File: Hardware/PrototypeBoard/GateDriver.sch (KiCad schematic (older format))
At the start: 38 parts, among them U4 TLE7185-1E

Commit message: continued to work on new layout
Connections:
- net Source_V_L: now also U4.24 (SL2)
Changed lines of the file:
@@
 Wire Wire Line
 	6950 3700 7300 3700
+Wire Wire Line
+	5700 4800 6300 4800
 $EndSCHEMATC

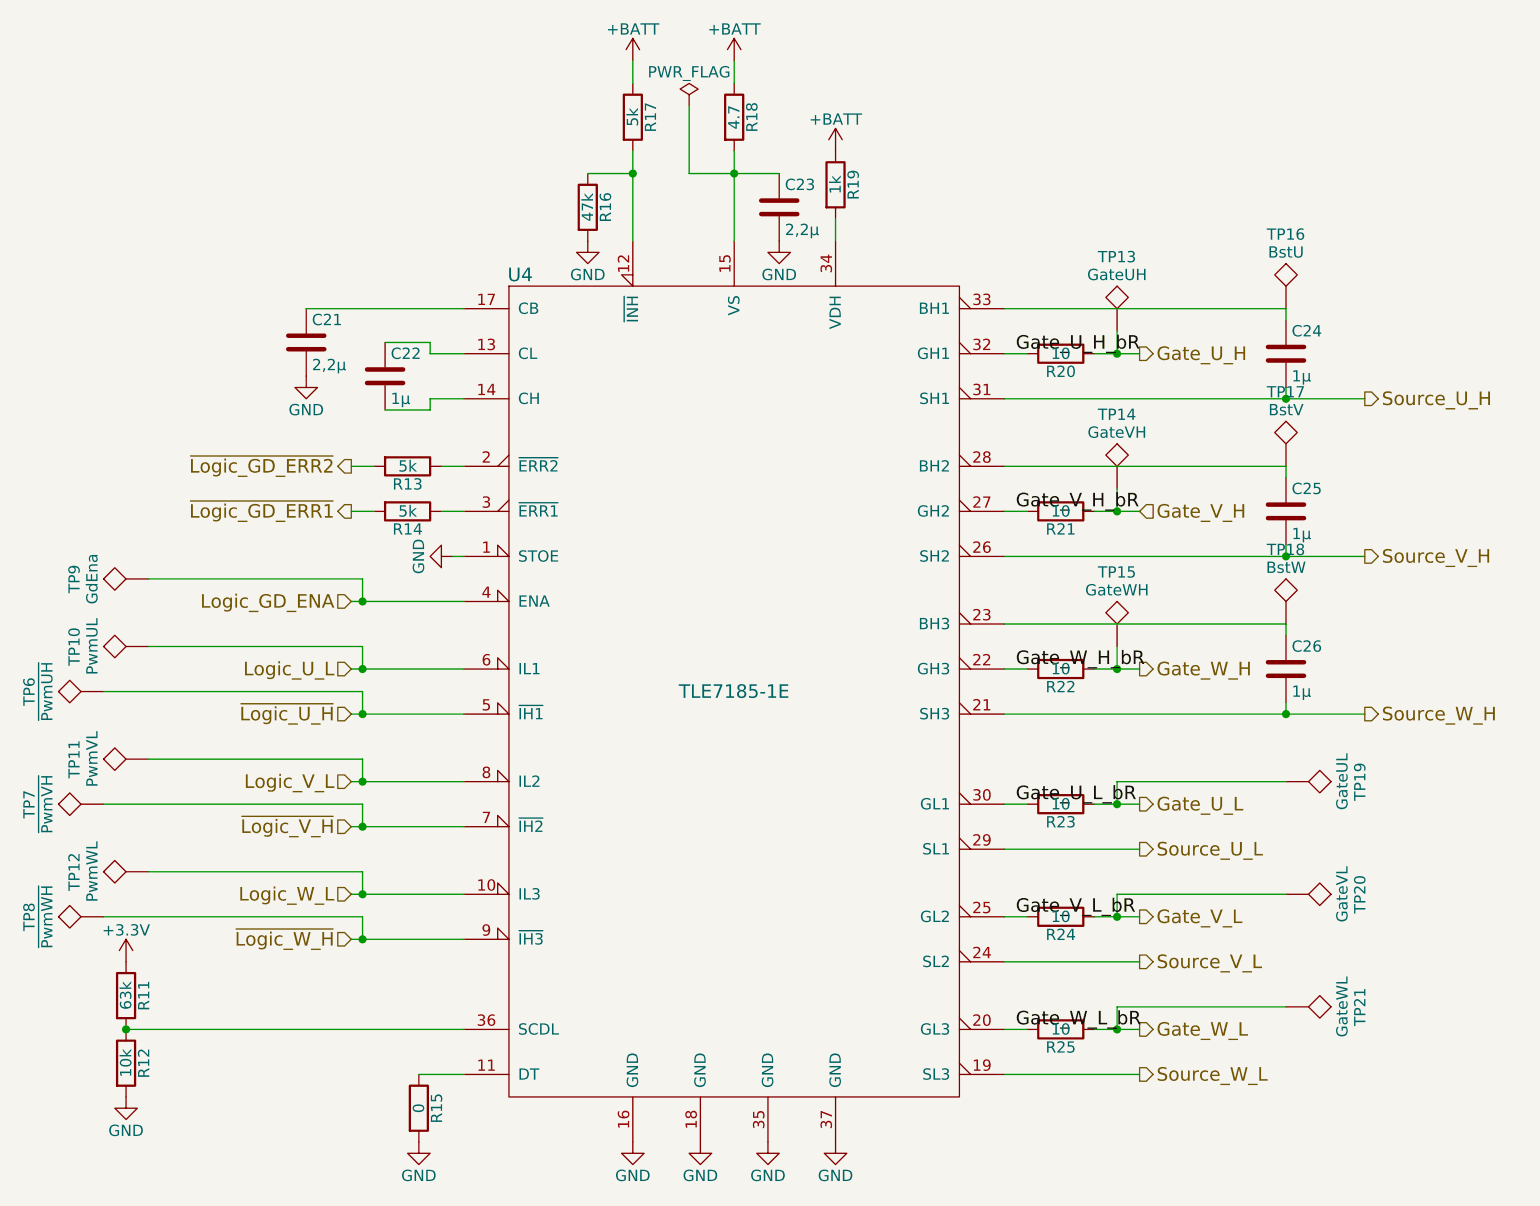
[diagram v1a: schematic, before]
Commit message: Added LEDs for PWM, SPI communication, Gate Driver Errors and Gate Driver disabled
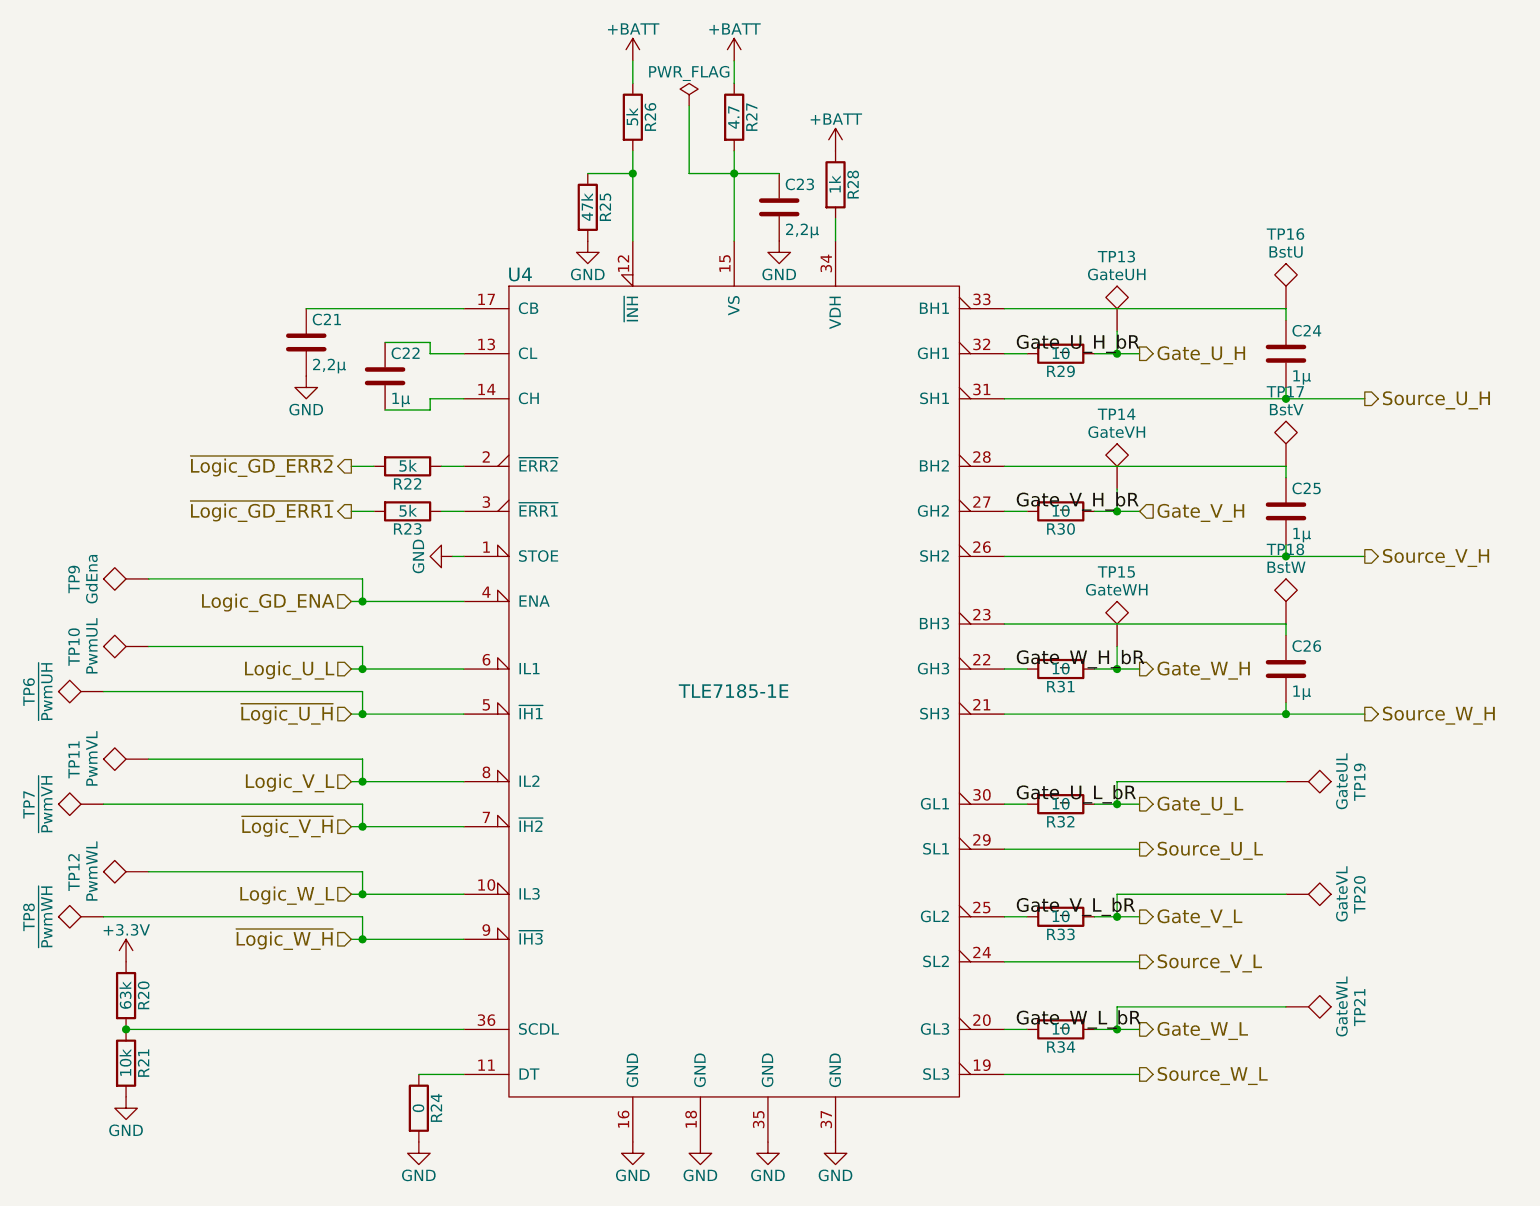
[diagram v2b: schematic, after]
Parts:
- renumbered R11 to R20, R12 to R21, R13 to R22, R14 to R23, R15 to R24, R16 to R25, R17 to R26, R18 to R27, R19 to R28, R20 to R29, R21 to R30, R22 to R31, R23 to R32, R24 to R33, R25 to R34
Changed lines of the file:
@@
 Logic_GD_ENA
 $Comp
-L Device:R R14
+L Device:R R23
 U 1 1 56C25790
 P 3050 2800
-F 0 "R14" V 3130 2800 50  0000 C CNN
+F 0 "R23" V 3130 2800 50  0000 C CNN
 F 1 "5k" V 3050 2800 50  0000 C CNN
 F 2 "Resistors_SMD:R_0805_HandSoldering" V 2980 2800 50  0001 C CNN
@@
 $EndComp
 $Comp
-L Device:R R13
+L Device:R R22
 U 1 1 56C257FB
 P 3050 2600
-F 0 "R13" V 3130 2600 50  0000 C CNN
+F 0 "R22" V 3130 2600 50  0000 C CNN
 F 1 "5k" V 3050 2600 50  0000 C CNN
 F 2 "Resistors_SMD:R_0805_HandSoldering" V 2980 2600 50  0001 C CNN
@@
 	2600 1900 3300 1900
 $Comp
-L power:GND #PWR038
+L power:GND #PWR044
 U 1 1 56C259AC
 P 2600 2200
-F 0 "#PWR038" H 2600 1950 50  0001 C CNN
+F 0 "#PWR044" H 2600 1950 50  0001 C CNN
 F 1 "GND" H 2600 2050 50  0000 C CNN
 F 2 "" H 2600 2200 50  0000 C CNN
@@
 $EndComp
 $Comp
-L Device:R R11
+L Device:R R20
 U 1 1 56C25A1A
 P 1800 4950
-F 0 "R11" V 1880 4950 50  0000 C CNN
+F 0 "R20" V 1880 4950 50  0000 C CNN
 F 1 "63k" V 1800 4950 50  0000 C CNN
 F 2 "Resistors_SMD:R_0805_HandSoldering" V 1730 4950 50  0001 C CNN
@@
 $EndComp
 $Comp
-L Device:R R12
+L Device:R R21
 U 1 1 56C25AD5
 P 1800 5250
-F 0 "R12" V 1880 5250 50  0000 C CNN
+F 0 "R21" V 1880 5250 50  0000 C CNN
 F 1 "10k" V 1800 5250 50  0000 C CNN
 F 2 "Resistors_SMD:R_0805_HandSoldering" V 1730 5250 50  0001 C CNN
@@
 $EndComp
 $Comp
-L Device:R R15
+L Device:R R24
 U 1 1 56C25B0C
 P 3100 5450
-F 0 "R15" V 3180 5450 50  0000 C CNN
+F 0 "R24" V 3180 5450 50  0000 C CNN
 F 1 "0" V 3100 5450 50  0000 C CNN
 F 2 "Resistors_SMD:R_0805_HandSoldering" V 3030 5450 50  0001 C CNN
@@
 	3300 5300 3100 5300
 $Comp
-L power:GND #PWR037
+L power:GND #PWR043
 U 1 1 56C25C22
 P 1800 5400
-F 0 "#PWR037" H 1800 5150 50  0001 C CNN
+F 0 "#PWR043" H 1800 5150 50  0001 C CNN
 F 1 "GND" H 1800 5250 50  0000 C CNN
 F 2 "" H 1800 5400 50  0000 C CNN
@@
 $EndComp
 $Comp
-L power:GND #PWR039
+L power:GND #PWR045
 U 1 1 56C25CA5
 P 3100 5600
-F 0 "#PWR039" H 3100 5350 50  0001 C CNN
+F 0 "#PWR045" H 3100 5350 50  0001 C CNN
 F 1 "GND" H 3100 5450 50  0000 C CNN
 F 2 "" H 3100 5600 50  0000 C CNN
@@
 $EndComp
 $Comp
-L power:+3.3V #PWR036
+L power:+3.3V #PWR042
 U 1 1 56C25D62
 P 1800 4800
-F 0 "#PWR036" H 1800 4650 50  0001 C CNN
+F 0 "#PWR042" H 1800 4650 50  0001 C CNN
 F 1 "+3.3V" H 1800 4940 50  0000 C CNN
 F 2 "" H 1800 4800 50  0000 C CNN
@@
 $EndComp
 $Comp
-L Device:R R18
+L Device:R R27
 U 1 1 56C25E1E
 P 4500 1050
-F 0 "R18" V 4580 1050 50  0000 C CNN
+F 0 "R27" V 4580 1050 50  0000 C CNN
 F 1 "4.7" V 4500 1050 50  0000 C CNN
 F 2 "Resistors_SMD:R_0805_HandSoldering" V 4430 1050 50  0001 C CNN
@@
 $EndComp
 $Comp
-L power:GND #PWR047
+L power:GND #PWR053
 U 1 1 56C2602E
 P 4700 1600
-F 0 "#PWR047" H 4700 1350 50  0001 C CNN
+F 0 "#PWR053" H 4700 1350 50  0001 C CNN
 F 1 "GND" H 4700 1450 50  0000 C CNN
 F 2 "" H 4700 1600 50  0000 C CNN
@@
 $EndComp
 $Comp
-L power:+BATT #PWR045
+L power:+BATT #PWR051
 U 1 1 56C261FD
 P 4500 800
-F 0 "#PWR045" H 4500 650 50  0001 C CNN
+F 0 "#PWR051" H 4500 650 50  0001 C CNN
 F 1 "+BATT" H 4500 940 50  0000 C CNN
 F 2 "" H 4500 800 50  0000 C CNN
@@
 $EndComp
 $Comp
-L Device:R R19
+L Device:R R28
 U 1 1 56C26356
 P 4950 1350
-F 0 "R19" V 5030 1350 50  0000 C CNN
+F 0 "R28" V 5030 1350 50  0000 C CNN
 F 1 "1k" V 4950 1350 50  0000 C CNN
 F 2 "Resistors_SMD:R_0805_HandSoldering" V 4880 1350 50  0001 C CNN
@@
 	4950 1500 4950 1600
 $Comp
-L power:+BATT #PWR048
+L power:+BATT #PWR054
 U 1 1 56C26408
 P 4950 1200
-F 0 "#PWR048" H 4950 1050 50  0001 C CNN
+F 0 "#PWR054" H 4950 1050 50  0001 C CNN
 F 1 "+BATT" H 4950 1340 50  0000 C CNN
 F 2 "" H 4950 1200 50  0000 C CNN
@@
 Gate_W_L
 $Comp
-L Device:R R25
+L Device:R R34
 U 1 1 56C2703F
 P 5950 5100
-F 0 "R25" V 6030 5100 50  0000 C CNN
+F 0 "R34" V 6030 5100 50  0000 C CNN
 F 1 "10" V 5950 5100 50  0000 C CNN
 F 2 "Resistors_SMD:R_0805_HandSoldering" V 5880 5100 50  0001 C CNN
@@
 $EndComp
 $Comp
-L Device:R R24
+L Device:R R33
 U 1 1 56C271C9
 P 5950 4600
-F 0 "R24" V 6030 4600 50  0000 C CNN
+F 0 "R33" V 6030 4600 50  0000 C CNN
 F 1 "10" V 5950 4600 50  0000 C CNN
 F 2 "Resistors_SMD:R_0805_HandSoldering" V 5880 4600 50  0001 C CNN
@@
 Gate_U_L
 $Comp
-L Device:R R23
+L Device:R R32
 U 1 1 56C27221
 P 5950 4100
-F 0 "R23" V 6030 4100 50  0000 C CNN
+F 0 "R32" V 6030 4100 50  0000 C CNN
 F 1 "10" V 5950 4100 50  0000 C CNN
 F 2 "Resistors_SMD:R_0805_HandSoldering" V 5880 4100 50  0001 C CNN
@@
 $EndComp
 $Comp
-L Device:R R22
+L Device:R R31
 U 1 1 56C2752F
 P 5950 3500
-F 0 "R22" V 6030 3500 50  0000 C CNN
+F 0 "R31" V 6030 3500 50  0000 C CNN
 F 1 "10" V 5950 3500 50  0000 C CNN
 F 2 "Resistors_SMD:R_0805_HandSoldering" V 5880 3500 50  0001 C CNN
@@
 $EndComp
 $Comp
-L Device:R R21
+L Device:R R30
 U 1 1 56C2759F
 P 5950 2800
-F 0 "R21" V 6030 2800 50  0000 C CNN
+F 0 "R30" V 6030 2800 50  0000 C CNN
 F 1 "10" V 5950 2800 50  0000 C CNN
 F 2 "Resistors_SMD:R_0805_HandSoldering" V 5880 2800 50  0001 C CNN
@@
 $EndComp
 $Comp
-L Device:R R20
+L Device:R R29
 U 1 1 56C27617
 P 5950 2100
-F 0 "R20" V 6030 2100 50  0000 C CNN
+F 0 "R29" V 6030 2100 50  0000 C CNN
 F 1 "10" V 5950 2100 50  0000 C CNN
 F 2 "Resistors_SMD:R_0805_HandSoldering" V 5880 2100 50  0001 C CNN
@@
 $EndComp
 $Comp
-L power:GND #PWR043
+L power:GND #PWR049
 U 1 1 56C35C82
 P 4050 5600
-F 0 "#PWR043" H 4050 5350 50  0001 C CNN
+F 0 "#PWR049" H 4050 5350 50  0001 C CNN
 F 1 "GND" H 4050 5450 50  0000 C CNN
 F 2 "" H 4050 5600 50  0000 C CNN
@@
 $EndComp
 $Comp
-L power:GND #PWR044
+L power:GND #PWR050
 U 1 1 56C35CC9
 P 4350 5600
-F 0 "#PWR044" H 4350 5350 50  0001 C CNN
+F 0 "#PWR050" H 4350 5350 50  0001 C CNN
 F 1 "GND" H 4350 5450 50  0000 C CNN
 F 2 "" H 4350 5600 50  0000 C CNN
@@
 $EndComp
 $Comp
-L power:GND #PWR046
+L power:GND #PWR052
 U 1 1 56C35D10
 P 4650 5600
-F 0 "#PWR046" H 4650 5350 50  0001 C CNN
+F 0 "#PWR052" H 4650 5350 50  0001 C CNN
 F 1 "GND" H 4650 5450 50  0000 C CNN
 F 2 "" H 4650 5600 50  0000 C CNN
@@
 $EndComp
 $Comp
-L power:GND #PWR049
+L power:GND #PWR055
 U 1 1 56C35D57
 P 4950 5600
-F 0 "#PWR049" H 4950 5350 50  0001 C CNN
+F 0 "#PWR055" H 4950 5350 50  0001 C CNN
 F 1 "GND" H 4950 5450 50  0000 C CNN
 F 2 "" H 4950 5600 50  0000 C CNN
@@
 $EndComp
 $Comp
-L Device:R R16
+L Device:R R25
 U 1 1 56C36A2B
 P 3850 1450
-F 0 "R16" V 3930 1450 50  0000 C CNN
+F 0 "R25" V 3930 1450 50  0000 C CNN
 F 1 "47k" V 3850 1450 50  0000 C CNN
 F 2 "Resistors_SMD:R_0805_HandSoldering" V 3780 1450 50  0001 C CNN
@@
 $EndComp
 $Comp
-L power:GND #PWR041
+L power:GND #PWR047
 U 1 1 56C36B52
 P 3850 1600
-F 0 "#PWR041" H 3850 1350 50  0001 C CNN
+F 0 "#PWR047" H 3850 1350 50  0001 C CNN
 F 1 "GND" H 3850 1450 50  0000 C CNN
 F 2 "" H 3850 1600 50  0000 C CNN
@@
 $EndComp
 $Comp
-L Device:R R17
+L Device:R R26
 U 1 1 56C36CC4
 P 4050 1050
-F 0 "R17" V 4130 1050 50  0000 C CNN
+F 0 "R26" V 4130 1050 50  0000 C CNN
 F 1 "5k" V 4050 1050 50  0000 C CNN
 F 2 "Resistors_SMD:R_0805_HandSoldering" V 3980 1050 50  0001 C CNN
@@
 $EndComp
 $Comp
-L power:+BATT #PWR042
+L power:+BATT #PWR048
 U 1 1 56C36FE8
 P 4050 800
-F 0 "#PWR042" H 4050 650 50  0001 C CNN
+F 0 "#PWR048" H 4050 650 50  0001 C CNN
 F 1 "+BATT" H 4050 940 50  0000 C CNN
 F 2 "" H 4050 800 50  0000 C CNN
@@
 Gate_U_H
 $Comp
-L power:GND #PWR040
+L power:GND #PWR046
 U 1 1 5AFC4218
 P 3250 3000
-F 0 "#PWR040" H 3250 2750 50  0001 C CNN
+F 0 "#PWR046" H 3250 2750 50  0001 C CNN
 F 1 "GND" H 3250 2850 50  0000 C CNN
 F 2 "" H 3250 3000 50  0000 C CNN

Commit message: All tracks routed, fixed bug in schematic, smaller test points
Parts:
- TP10, TP11, TP12, TP13, TP14, TP15, TP16, TP17, TP18, TP19, TP20, TP21, TP6, TP7, TP8, TP9: footprint Pin_Headers:Pin_Header_Straight_1x01_Pitch2.00mm -> Pin_Headers:Pin_Header_Straight_1x01_Pitch1.00mm
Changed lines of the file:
@@
 F 0 "TP17" H 6950 2900 50  0000 C BNN
 F 1 "BstV" H 6950 2850 50  0000 C CNN
-F 2 "Pin_Headers:Pin_Header_Straight_1x01_Pitch2.00mm" H 6950 2600 50  0001 C CNN
+F 2 "Pin_Headers:Pin_Header_Straight_1x01_Pitch1.00mm" H 6950 2600 50  0001 C CNN
 F 3 "" H 6950 2600 50  0001 C CNN
 	1    6950 2600
@@
 F 0 "TP16" H 6950 2200 50  0000 C BNN
 F 1 "BstU" H 6950 2150 50  0000 C CNN
-F 2 "Pin_Headers:Pin_Header_Straight_1x01_Pitch2.00mm" H 6950 1900 50  0001 C CNN
+F 2 "Pin_Headers:Pin_Header_Straight_1x01_Pitch1.00mm" H 6950 1900 50  0001 C CNN
 F 3 "" H 6950 1900 50  0001 C CNN
 	1    6950 1900
@@
 F 0 "TP18" H 6950 3600 50  0000 C BNN
 F 1 "BstW" H 6950 3550 50  0000 C CNN
-F 2 "Pin_Headers:Pin_Header_Straight_1x01_Pitch2.00mm" H 6950 3300 50  0001 C CNN
+F 2 "Pin_Headers:Pin_Header_Straight_1x01_Pitch1.00mm" H 6950 3300 50  0001 C CNN
 F 3 "" H 6950 3300 50  0001 C CNN
 	1    6950 3300
@@
 F 0 "TP14" H 6200 3000 50  0000 C BNN
 F 1 "GateVH" H 6200 2950 50  0000 C CNN
-F 2 "Pin_Headers:Pin_Header_Straight_1x01_Pitch2.00mm" H 6200 2700 50  0001 C CNN
+F 2 "Pin_Headers:Pin_Header_Straight_1x01_Pitch1.00mm" H 6200 2700 50  0001 C CNN
 F 3 "" H 6200 2700 50  0001 C CNN
 	1    6200 2700
@@
 F 0 "TP13" H 6200 2300 50  0000 C BNN
 F 1 "GateUH" H 6200 2250 50  0000 C CNN
-F 2 "Pin_Headers:Pin_Header_Straight_1x01_Pitch2.00mm" H 6200 2000 50  0001 C CNN
+F 2 "Pin_Headers:Pin_Header_Straight_1x01_Pitch1.00mm" H 6200 2000 50  0001 C CNN
 F 3 "" H 6200 2000 50  0001 C CNN
 	1    6200 2000
@@
 F 0 "TP15" H 6200 3700 50  0000 C BNN
 F 1 "GateWH" H 6200 3650 50  0000 C CNN
-F 2 "Pin_Headers:Pin_Header_Straight_1x01_Pitch2.00mm" H 6200 3400 50  0001 C CNN
+F 2 "Pin_Headers:Pin_Header_Straight_1x01_Pitch1.00mm" H 6200 3400 50  0001 C CNN
 F 3 "" H 6200 3400 50  0001 C CNN
 	1    6200 3400
@@
 F 0 "TP19" H 6950 4300 50  0000 C BNN
 F 1 "GateUL" H 6950 4250 50  0000 C CNN
-F 2 "Pin_Headers:Pin_Header_Straight_1x01_Pitch2.00mm" H 6950 4000 50  0001 C CNN
+F 2 "Pin_Headers:Pin_Header_Straight_1x01_Pitch1.00mm" H 6950 4000 50  0001 C CNN
 F 3 "" H 6950 4000 50  0001 C CNN
 	1    6950 4000
@@
 F 0 "TP20" H 6950 4800 50  0000 C BNN
 F 1 "GateVL" H 6950 4750 50  0000 C CNN
-F 2 "Pin_Headers:Pin_Header_Straight_1x01_Pitch2.00mm" H 6950 4500 50  0001 C CNN
+F 2 "Pin_Headers:Pin_Header_Straight_1x01_Pitch1.00mm" H 6950 4500 50  0001 C CNN
 F 3 "" H 6950 4500 50  0001 C CNN
 	1    6950 4500
@@
 F 0 "TP21" H 6950 5300 50  0000 C BNN
 F 1 "GateWL" H 6950 5250 50  0000 C CNN
-F 2 "Pin_Headers:Pin_Header_Straight_1x01_Pitch2.00mm" H 6950 5000 50  0001 C CNN
+F 2 "Pin_Headers:Pin_Header_Straight_1x01_Pitch1.00mm" H 6950 5000 50  0001 C CNN
 F 3 "" H 6950 5000 50  0001 C CNN
 	1    6950 5000
@@
 F 0 "TP9" H 1900 3400 50  0000 C BNN
 F 1 "GdEna" H 1900 3350 50  0000 C CNN
-F 2 "Pin_Headers:Pin_Header_Straight_1x01_Pitch2.00mm" H 1900 3100 50  0001 C CNN
+F 2 "Pin_Headers:Pin_Header_Straight_1x01_Pitch1.00mm" H 1900 3100 50  0001 C CNN
 F 3 "" H 1900 3100 50  0001 C CNN
 	1    1900 3100
@@
 F 0 "TP10" H 1900 3700 50  0000 C BNN
 F 1 "PwmUL" H 1900 3650 50  0000 C CNN
-F 2 "Pin_Headers:Pin_Header_Straight_1x01_Pitch2.00mm" H 1900 3400 50  0001 C CNN
+F 2 "Pin_Headers:Pin_Header_Straight_1x01_Pitch1.00mm" H 1900 3400 50  0001 C CNN
 F 3 "" H 1900 3400 50  0001 C CNN
 	1    1900 3400
@@
 F 0 "TP6" H 1700 3900 50  0000 C BNN
 F 1 "~PwmUH" H 1700 3850 50  0000 C CNN
-F 2 "Pin_Headers:Pin_Header_Straight_1x01_Pitch2.00mm" H 1700 3600 50  0001 C CNN
+F 2 "Pin_Headers:Pin_Header_Straight_1x01_Pitch1.00mm" H 1700 3600 50  0001 C CNN
 F 3 "" H 1700 3600 50  0001 C CNN
 	1    1700 3600
@@
 F 0 "TP11" H 1900 4200 50  0000 C BNN
 F 1 "PwmVL" H 1900 4150 50  0000 C CNN
-F 2 "Pin_Headers:Pin_Header_Straight_1x01_Pitch2.00mm" H 1900 3900 50  0001 C CNN
+F 2 "Pin_Headers:Pin_Header_Straight_1x01_Pitch1.00mm" H 1900 3900 50  0001 C CNN
 F 3 "" H 1900 3900 50  0001 C CNN
 	1    1900 3900
@@
 F 0 "TP7" H 1700 4400 50  0000 C BNN
 F 1 "~PwmVH" H 1700 4350 50  0000 C CNN
-F 2 "Pin_Headers:Pin_Header_Straight_1x01_Pitch2.00mm" H 1700 4100 50  0001 C CNN
+F 2 "Pin_Headers:Pin_Header_Straight_1x01_Pitch1.00mm" H 1700 4100 50  0001 C CNN
 F 3 "" H 1700 4100 50  0001 C CNN
 	1    1700 4100
@@
 F 0 "TP12" H 1900 4700 50  0000 C BNN
 F 1 "PwmWL" H 1900 4650 50  0000 C CNN
-F 2 "Pin_Headers:Pin_Header_Straight_1x01_Pitch2.00mm" H 1900 4400 50  0001 C CNN
+F 2 "Pin_Headers:Pin_Header_Straight_1x01_Pitch1.00mm" H 1900 4400 50  0001 C CNN
 F 3 "" H 1900 4400 50  0001 C CNN
 	1    1900 4400
@@
 F 0 "TP8" H 1700 4900 50  0000 C BNN
 F 1 "~PwmWH" H 1700 4850 50  0000 C CNN
-F 2 "Pin_Headers:Pin_Header_Straight_1x01_Pitch2.00mm" H 1700 4600 50  0001 C CNN
+F 2 "Pin_Headers:Pin_Header_Straight_1x01_Pitch1.00mm" H 1700 4600 50  0001 C CNN
 F 3 "" H 1700 4600 50  0001 C CNN
 	1    1700 4600
